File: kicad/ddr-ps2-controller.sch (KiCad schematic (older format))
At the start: 36 parts, among them J1 BTN0, J2 BTN1, J3 BTN2, J4 BTN3, J5 ISCP, J6 PS2, J7 BTN4, J8 BTN5/UPSTREAM, Q1 DMN63D8LDW, U1 ATtiny20-MMH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

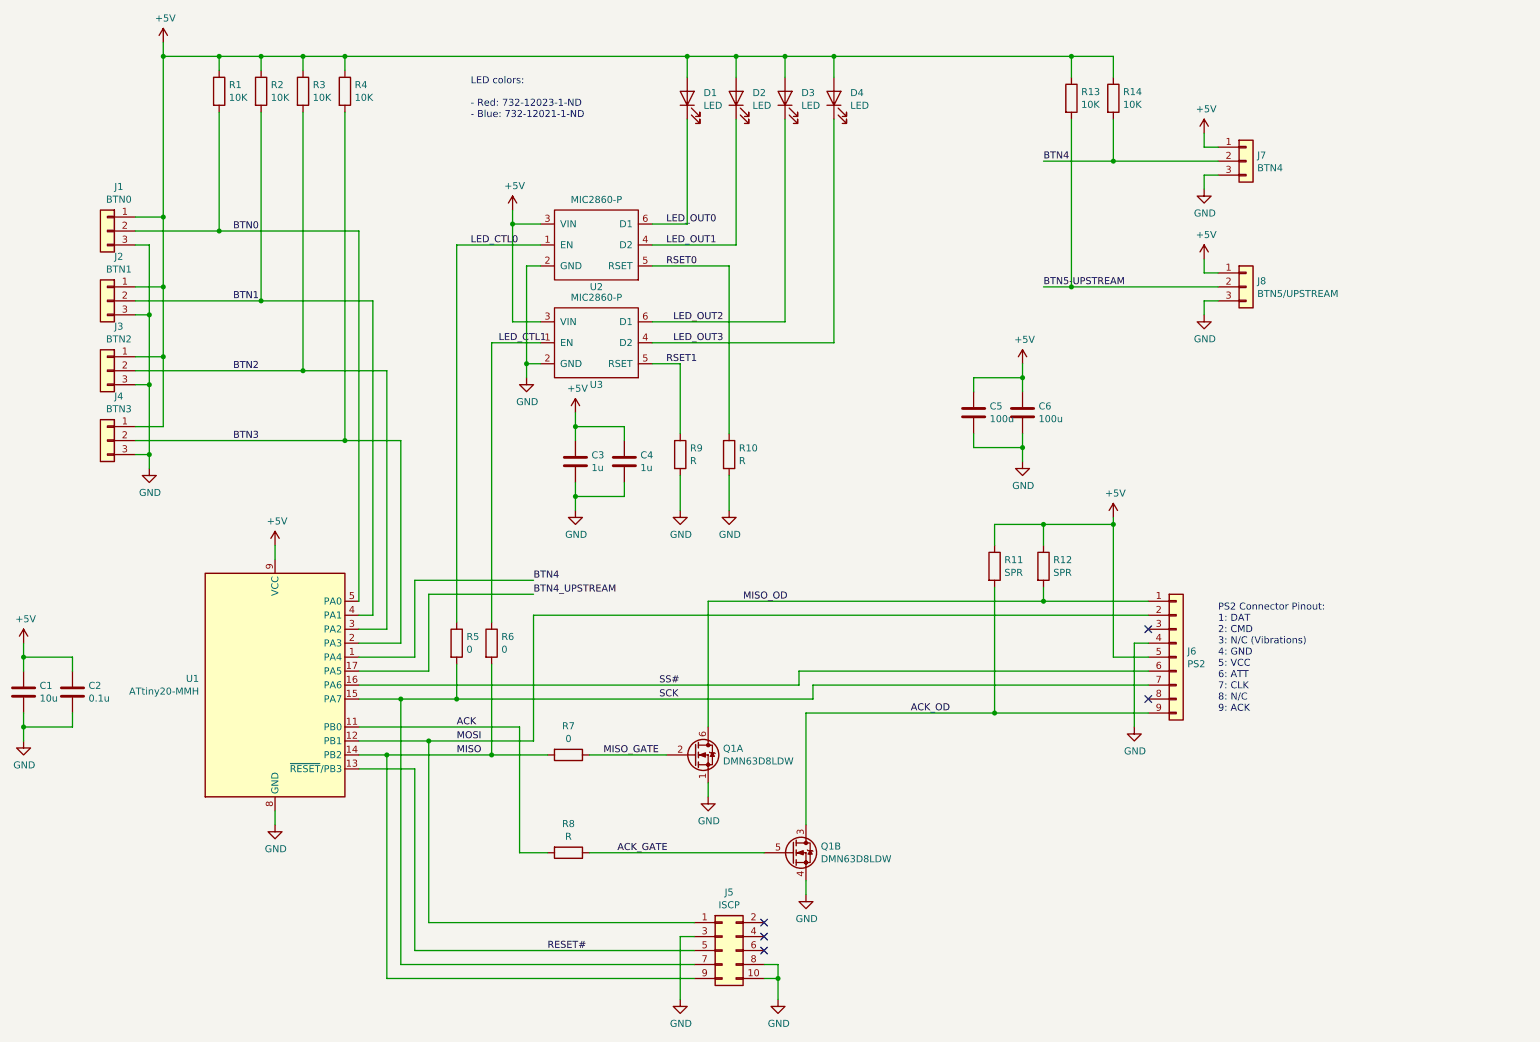
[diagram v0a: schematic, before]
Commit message: Initial PCB layout with CAD files for new footprints
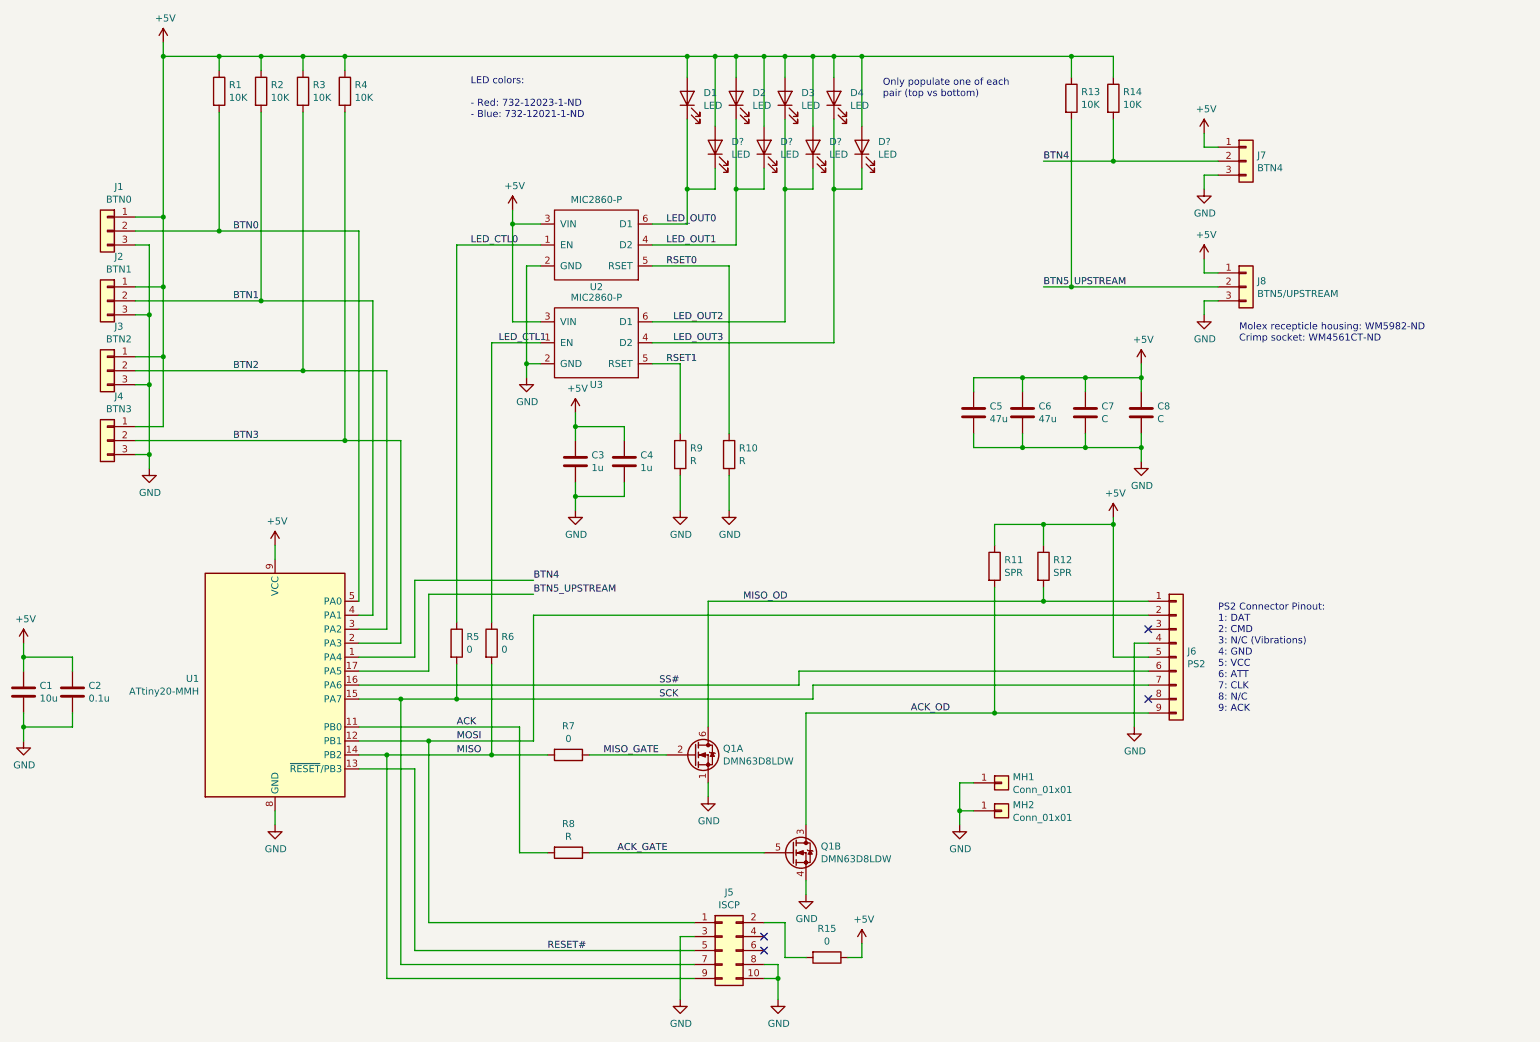
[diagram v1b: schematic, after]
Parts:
- added C7, C8: C, Capacitor_SMD:C_0805_2012Metric, symbol Device:C
- added D? (x4): LED, ddr-ps2-controller:Wurth_WL-SMSW_LED, symbol Device:LED
- added MH1, MH2: Conn_01x01, MountingHole:MountingHole_4.3mm_M4_Pad_Via, symbol Connector_Generic:Conn_01x01
- added R15: 0, Resistor_SMD:R_0603_1608Metric, symbol Device:R
- C5, C6: value 100u -> 47u; Part Number (none) -> 587-1780-1-ND
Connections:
- net BTN5-UPSTREAM is gone; now on net BTN5_UPSTREAM: J8.2 (Pin_2), R13.2
- net +5V: now also C7.1, C8.1, D?.2 (A), D?.2 (A), D?.2 (A), D?.2 (A), R15.1
- net GND: now also C7.2, C8.2, MH1.1 (Pin_1), MH2.1 (Pin_1)
- net LED_OUT0: now also D?.1 (K)
- net LED_OUT1: now also D?.1 (K)
- net LED_OUT2: now also D?.1 (K)
- net LED_OUT3: now also D?.1 (K)
- net at J5.2 (Pin_2): now also R15.2
- net BTN4_UPSTREAM renamed BTN5_UPSTREAM
- no-connect marks 5 -> 4
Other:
- note added: "Molex recepticle housing: WM5982-ND\nCrimp socket: WM4561CT-ND"
- note added: "Only populate one of each\npair (top vs bottom)"

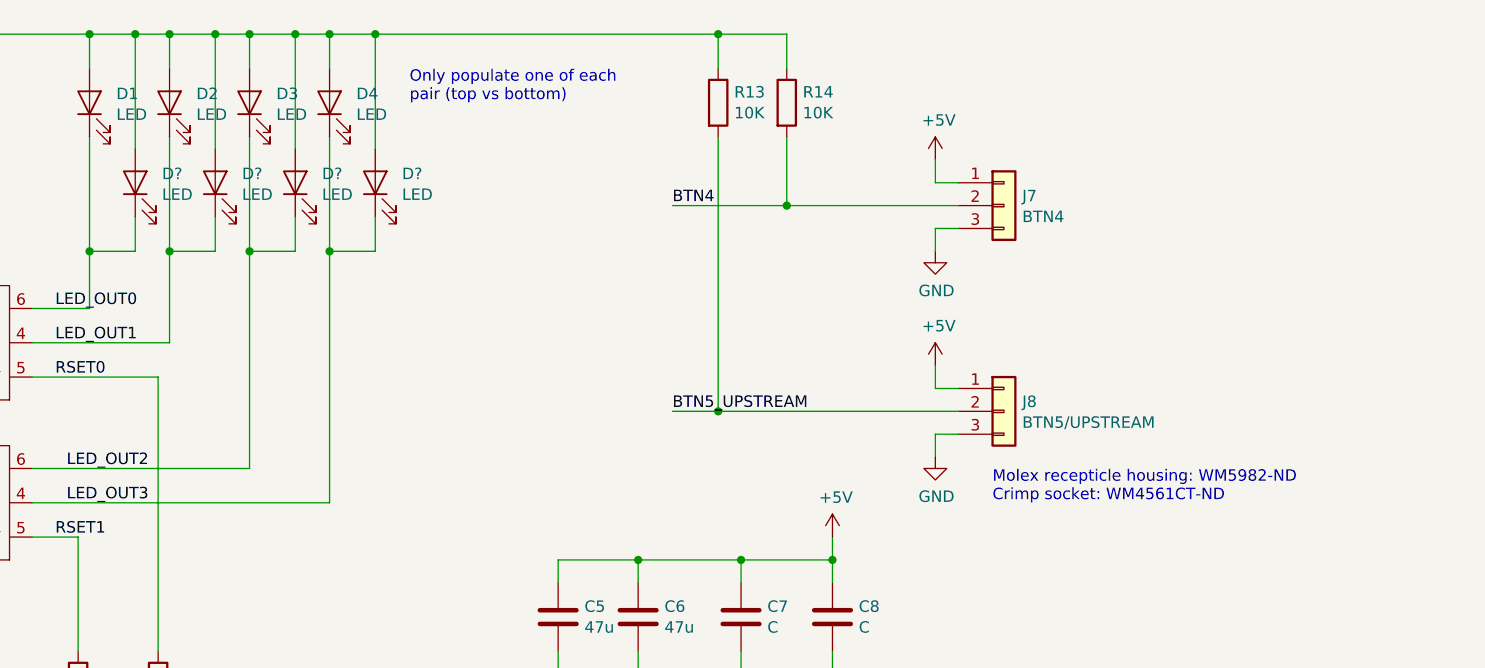
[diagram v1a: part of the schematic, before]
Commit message: Changed connector to the far cheaper JST-EH
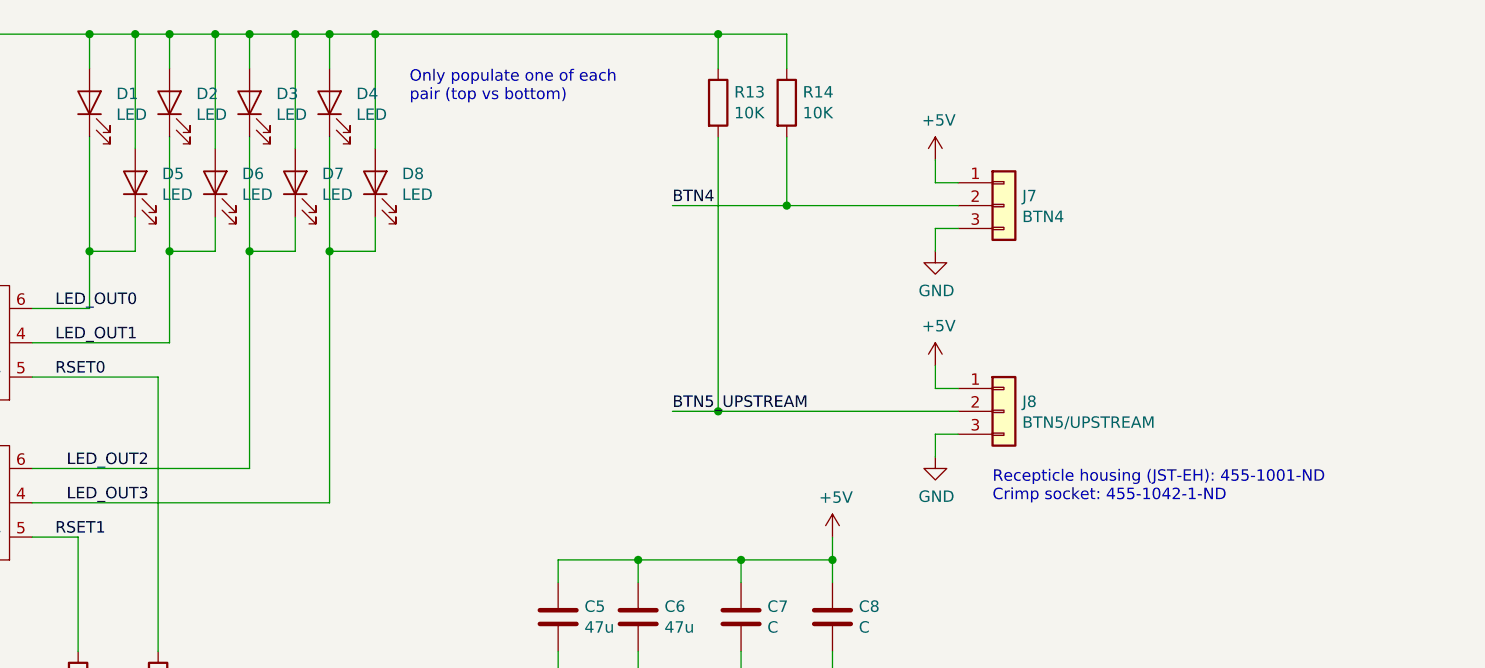
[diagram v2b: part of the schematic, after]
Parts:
- J1, J2, J3, J4, J7, J8: footprint ddr-ps2-controller:Molex_35363_2mm_RA -> ddr-ps2-controller:JST_EH_3_RA; Part Number WM18932-ND -> 455-1626-ND‎
- gave numbers to parts that had none: 4
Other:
- note added: "Recepticle housing (JST-EH): 455-1001-ND‎\nCrimp socket: 455-1042-1-ND‎"
- note removed: "Molex recepticle housing: WM5982-ND\nCrimp socket: WM4561CT-ND"
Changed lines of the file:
@@
 F 0 "J1" H 1218 2367 50  0000 C CNN
 F 1 "BTN0" H 1218 2276 50  0000 C CNN
-F 2 "ddr-ps2-controller:Molex_35363_2mm_RA" H 1300 2050 50  0001 C CNN
+F 2 "ddr-ps2-controller:JST_EH_3_RA" H 1300 2050 50  0001 C CNN
 F 3 "~" H 1300 2050 50  0001 C CNN
-F 4 "WM18932-ND" H 1300 2050 50  0001 C CNN "Part Number"
+F 4 "455-1626-ND‎" H 1300 2050 50  0001 C CNN "Part Number"
 	1    1300 2050
 	-1   0    0    -1
@@
 F 0 "J2" H 1218 2867 50  0000 C CNN
 F 1 "BTN1" H 1218 2776 50  0000 C CNN
-F 2 "ddr-ps2-controller:Molex_35363_2mm_RA" H 1300 2550 50  0001 C CNN
+F 2 "ddr-ps2-controller:JST_EH_3_RA" H 1300 2550 50  0001 C CNN
 F 3 "~" H 1300 2550 50  0001 C CNN
-F 4 "WM18932-ND" H 1300 2550 50  0001 C CNN "Part Number"
+F 4 "455-1626-ND‎" H 1300 2550 50  0001 C CNN "Part Number"
 	1    1300 2550
 	-1   0    0    -1
@@
 F 0 "J3" H 1218 3367 50  0000 C CNN
 F 1 "BTN2" H 1218 3276 50  0000 C CNN
-F 2 "ddr-ps2-controller:Molex_35363_2mm_RA" H 1300 3050 50  0001 C CNN
+F 2 "ddr-ps2-controller:JST_EH_3_RA" H 1300 3050 50  0001 C CNN
 F 3 "~" H 1300 3050 50  0001 C CNN
-F 4 "WM18932-ND" H 1300 3050 50  0001 C CNN "Part Number"
+F 4 "455-1626-ND‎" H 1300 3050 50  0001 C CNN "Part Number"
 	1    1300 3050
 	-1   0    0    -1
@@
 F 0 "J4" H 1218 3867 50  0000 C CNN
 F 1 "BTN3" H 1218 3776 50  0000 C CNN
-F 2 "ddr-ps2-controller:Molex_35363_2mm_RA" H 1300 3550 50  0001 C CNN
+F 2 "ddr-ps2-controller:JST_EH_3_RA" H 1300 3550 50  0001 C CNN
 F 3 "~" H 1300 3550 50  0001 C CNN
-F 4 "WM18932-ND" H 1300 3550 50  0001 C CNN "Part Number"
+F 4 "455-1626-ND‎" H 1300 3550 50  0001 C CNN "Part Number"
 	1    1300 3550
 	-1   0    0    -1
@@
 F 0 "J7" H 9530 1592 50  0000 L CNN
 F 1 "BTN4" H 9530 1501 50  0000 L CNN
-F 2 "ddr-ps2-controller:Molex_35363_2mm_RA" H 9450 1550 50  0001 C CNN
+F 2 "ddr-ps2-controller:JST_EH_3_RA" H 9450 1550 50  0001 C CNN
 F 3 "~" H 9450 1550 50  0001 C CNN
-F 4 "WM18932-ND" H 9450 1550 50  0001 C CNN "Part Number"
+F 4 "455-1626-ND‎" H 9450 1550 50  0001 C CNN "Part Number"
 	1    9450 1550
 	1    0    0    -1
@@
 F 0 "J8" H 9530 2492 50  0000 L CNN
 F 1 "BTN5/UPSTREAM" H 9530 2401 50  0000 L CNN
-F 2 "ddr-ps2-controller:Molex_35363_2mm_RA" H 9450 2450 50  0001 C CNN
+F 2 "ddr-ps2-controller:JST_EH_3_RA" H 9450 2450 50  0001 C CNN
 F 3 "~" H 9450 2450 50  0001 C CNN
-F 4 "WM18932-ND" H 9450 2450 50  0001 C CNN "Part Number"
+F 4 "455-1626-ND‎" H 9450 2450 50  0001 C CNN "Part Number"
 	1    9450 2450
 	1    0    0    -1
@@
 	7850 3100 7850 3200
 Text Notes 9400 2850 0    50   ~ 0
-Molex recepticle housing: WM5982-ND\nCrimp socket: WM4561CT-ND
+Recepticle housing (JST-EH): 455-1001-ND‎\nCrimp socket: 455-1042-1-ND‎
 $Comp
 L Connector_Generic:Conn_01x01 MH1
@@
 	6150 7250 6300 7250
 $Comp
-L Device:LED D?
+L Device:LED D5
 U 1 1 5D12D171
 P 5650 1450
-F 0 "D?" V 5689 1333 50  0000 R CNN
+F 0 "D5" V 5689 1333 50  0000 R CNN
 F 1 "LED" V 5598 1333 50  0000 R CNN
 F 2 "ddr-ps2-controller:Wurth_WL-SMSW_LED" H 5650 1450 50  0001 C CNN
@@
 $EndComp
 $Comp
-L Device:LED D?
+L Device:LED D6
 U 1 1 5D12D178
 P 6000 1450
-F 0 "D?" V 6039 1333 50  0000 R CNN
+F 0 "D6" V 6039 1333 50  0000 R CNN
 F 1 "LED" V 5948 1333 50  0000 R CNN
 F 2 "ddr-ps2-controller:Wurth_WL-SMSW_LED" H 6000 1450 50  0001 C CNN
@@
 $EndComp
 $Comp
-L Device:LED D?
+L Device:LED D7
 U 1 1 5D12D17F
 P 6350 1450
-F 0 "D?" V 6389 1333 50  0000 R CNN
+F 0 "D7" V 6389 1333 50  0000 R CNN
 F 1 "LED" V 6298 1333 50  0000 R CNN
 F 2 "ddr-ps2-controller:Wurth_WL-SMSW_LED" H 6350 1450 50  0001 C CNN
@@
 $EndComp
 $Comp
-L Device:LED D?
+L Device:LED D8
 U 1 1 5D12D186
 P 6700 1450
-F 0 "D?" V 6739 1333 50  0000 R CNN
+F 0 "D8" V 6739 1333 50  0000 R CNN
 F 1 "LED" V 6648 1333 50  0000 R CNN
 F 2 "ddr-ps2-controller:Wurth_WL-SMSW_LED" H 6700 1450 50  0001 C CNN
